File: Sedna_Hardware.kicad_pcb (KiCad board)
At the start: 2 copper layers, 82.8 x 90.4 mm, 51 parts, among them J1 PJ-102A, J10 5-103735-2, J11 5-103634-1, J2 61201021721, J3 PPTC141LFBN-RC, J4 0878340619, J5 5-103634-2, J6 5-103361-1, J7 1935161, J8 1935161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

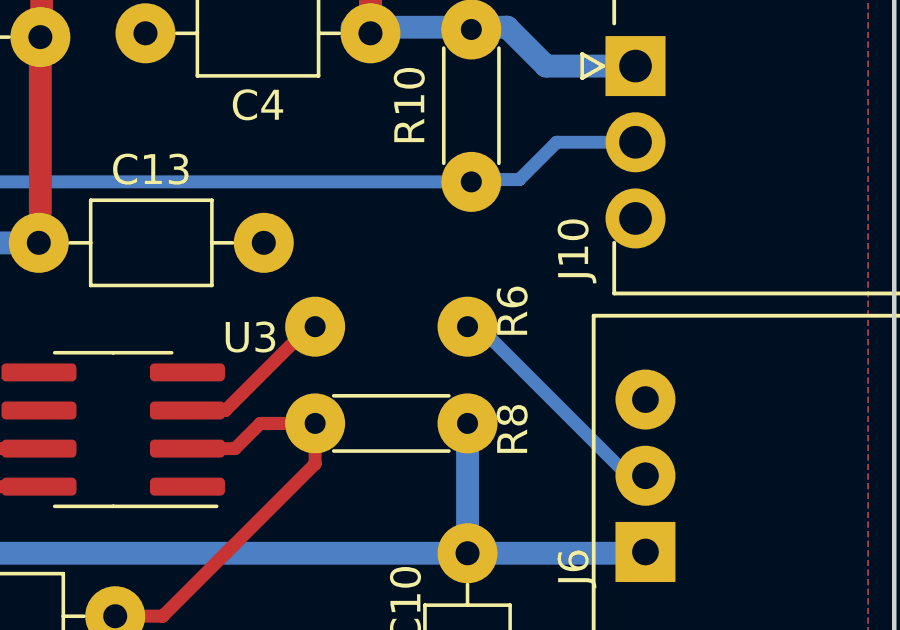
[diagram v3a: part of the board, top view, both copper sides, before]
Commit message: flipped resistor and power terminal to front plane
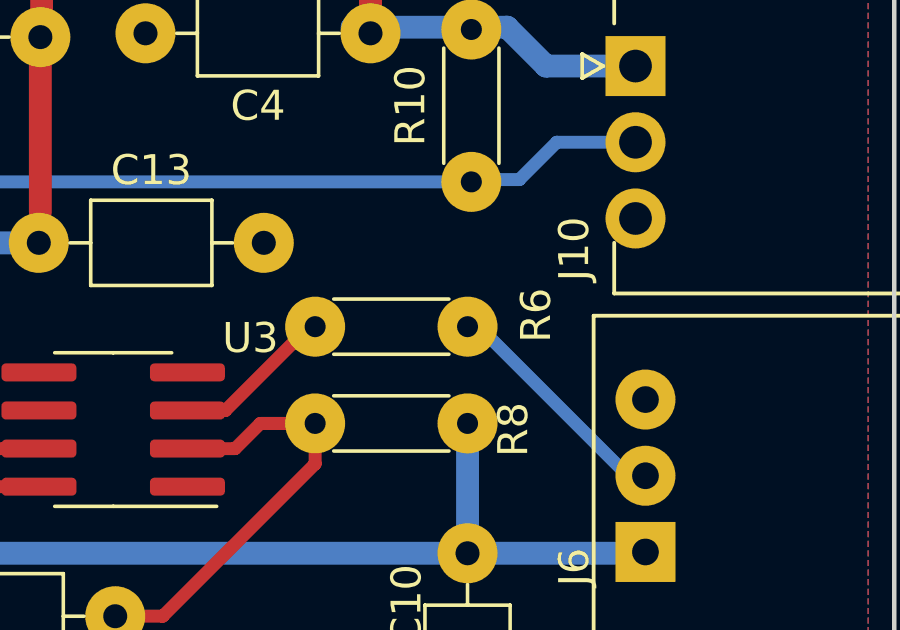
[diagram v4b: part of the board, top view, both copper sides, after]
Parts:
- R6: moved to F.Cu
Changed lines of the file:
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@@
+    )
+  )
+  (footprint "Resistor_THT:R_Axial_DIN0204_L3.6mm_D1.6mm_P5.08mm_Horizontal" (layer "F.Cu")
+    (at 171.176 128.347 180)
+    (descr "Resistor, Axial_DIN0204 series, Axial, Horizontal, pin pitch=5.08mm, 0.167W, length*diameter=3.6*1.6mm^2, http://cdn-reichelt.de/documents/datenblatt/B400/1_4W%23YAG.pdf")
+    (tags "Resistor Axial_DIN0204 series Axial Horizontal pin pitch 5.08mm 0.167W length 3.6mm diameter 1.6mm")
+    (property "Category" "Through Hole Resistors")
+    (property "DK_Datasheet_Link" "https://www.vishay.com/docs/28766/mbxsma.pdf")
+    (property "DK_Detail_Page" "https://www.digikey.ca/en/products/detail/vishay-beyschlag-draloric-bc-components/MBA02040C1002FRP00/336349")
+    (property "Description" "RES 10K OHM 0.4W 1% AXIAL")
+    (property "Digi-Key_PN" "BC10.0KXTR-ND")
+    (property "MPN" "MBA02040C1002FRP00")
+    (property "Manufacturer" "Vishay Beyschlag/Draloric/BC Components")
+    (property "Sheetfile" "Sedna_Hardware.kicad_sch")
+    (property "Sheetname" "")
+    (property "Status" "active")
+    (attr through_hole)
+    (fp_text reference "R6" (at -2.286 0.381 -90) (layer "F.SilkS")
+      (effects (font (size 1 1) (thickness 0.15)))
+    )
+    (fp_text value "10k" (at 2.54 1.92) (layer "F.Fab")
+      (effects (font (size 1 1) (thickness 0.15)))
+    )
+    (fp_text user "${REFERENCE}" (at 2.54 0) (layer "F.Fab")
+      (effects (font (size 0.72 0.72) (thickness 0.108)))
+    )
+    (fp_line (start 0.62 0.92) (end 4.46 0.92) (layer "F.SilkS") (width 0.12))
+    (fp_line (start 0.62 -0.92) (end 4.46 -0.92) (layer "F.SilkS") (width 0.12))
+    (fp_line (start 6.03 -1.05) (end -0.95 -1.05) (layer "F.CrtYd") (width 0.05))
+    (fp_line (start -0.95 -1.05) (end -0.95 1.05) (layer "F.CrtYd") (width 0.05))
+    (fp_line (start -0.95 1.05) (end 6.03 1.05) (layer "F.CrtYd") (width 0.05))
+    (fp_line (start 6.03 1.05) (end 6.03 -1.05) (layer "F.CrtYd") (width 0.05))
+    (fp_line (start 0.74 0.8) (end 4.34 0.8) (layer "F.Fab") (width 0.1))
+    (fp_line (start 0.74 -0.8) (end 0.74 0.8) (layer "F.Fab") (width 0.1))
+    (fp_line (start 5.08 0) (end 4.34 0) (layer "F.Fab") (width 0.1))
+    (fp_line (start 0 0) (end 0.74 0) (layer "F.Fab") (width 0.1))
+    (fp_line (start 4.34 -0.8) (end 0.74 -0.8) (layer "F.Fab") (width 0.1))
+    (fp_line (start 4.34 0.8) (end 4.34 -0.8) (layer "F.Fab") (width 0.1))
+    (pad "1" thru_hole circle (at 0 0 180) (size 2 2) (drill 0.7) (layers *.Cu *.Mask)
+      (net 21 "Net-(J6-Pad2)") (pintype "passive"))
+    (pad "2" thru_hole oval (at 5.08 0 180) (size 2 2) (drill 0.7) (layers *.Cu *.Mask)
+      (net 56 "Net-(R6-Pad2)") (pintype "passive"))
+    (model "${KICAD6_3DMODEL_DIR}/Resistor_THT.3dshapes/R_Axial_DIN0204_L3.6mm_D1.6mm_P5.08mm_Horizontal.wrl"
+      (offset (xyz 0 0 0))
+      (scale (xyz 1 1 1))
+      (rotate (xyz 0 0 0))
     )
   )
@@
       (net 35 "Net-(J7-Pad2)") (pintype "passive"))
   )
-  (footprint "Resistor_THT:R_Axial_DIN0204_L3.6mm_D1.6mm_P5.08mm_Horizontal" (layer "B.Cu")
-    (at 171.176 128.347 180)
-    (descr "Resistor, Axial_DIN0204 series, Axial, Horizontal, pin pitch=5.08mm, 0.167W, length*diameter=3.6*1.6mm^2, http://cdn-reichelt.de/documents/datenblatt/B400/1_4W%23YAG.pdf")
-    (tags "Resistor Axial_DIN0204 series Axial Horizontal pin pitch 5.08mm 0.167W length 3.6mm diameter 1.6mm")
-    (property "Category" "Through Hole Resistors")
-    (property "DK_Datasheet_Link" "https://www.vishay.com/docs/28766/mbxsma.pdf")
-    (property "DK_Detail_Page" "https://www.digikey.ca/en/products/detail/vishay-beyschlag-draloric-bc-components/MBA02040C1002FRP00/336349")
-    (property "Description" "RES 10K OHM 0.4W 1% AXIAL")
-    (property "Digi-Key_PN" "BC10.0KXTR-ND")
-    (property "MPN" "MBA02040C1002FRP00")
-    (property "Manufacturer" "Vishay Beyschlag/Draloric/BC Components")
-    (property "Sheetfile" "Sedna_Hardware.kicad_sch")
-    (property "Sheetname" "")
-    (property "Status" "active")
-    (attr through_hole)
-    (fp_text reference "R6" (at -1.524 0.508 90) (layer "F.SilkS")
-      (effects (font (size 1 1) (thickness 0.15)))
-    )
-    (fp_text value "10k" (at 2.54 -1.92) (layer "B.Fab")
-      (effects (font (size 1 1) (thickness 0.15)) (justify mirror))
-    )
-    (fp_text user "${REFERENCE}" (at 2.54 0) (layer "B.Fab")
-      (effects (font (size 0.72 0.72) (thickness 0.108)) (justify mirror))
-    )
-    (fp_line (start 0.62 -0.92) (end 4.46 -0.92) (layer "B.SilkS") (width 0.12))
-    (fp_line (start 0.62 0.92) (end 4.46 0.92) (layer "B.SilkS") (width 0.12))
-    (fp_line (start 6.03 1.05) (end -0.95 1.05) (layer "B.CrtYd") (width 0.05))
-    (fp_line (start -0.95 1.05) (end -0.95 -1.05) (layer "B.CrtYd") (width 0.05))
-    (fp_line (start -0.95 -1.05) (end 6.03 -1.05) (layer "B.CrtYd") (width 0.05))
-    (fp_line (start 6.03 -1.05) (end 6.03 1.05) (layer "B.CrtYd") (width 0.05))
-    (fp_line (start 0.74 -0.8) (end 4.34 -0.8) (layer "B.Fab") (width 0.1))
-    (fp_line (start 0.74 0.8) (end 0.74 -0.8) (layer "B.Fab") (width 0.1))
-    (fp_line (start 5.08 0) (end 4.34 0) (layer "B.Fab") (width 0.1))
-    (fp_line (start 0 0) (end 0.74 0) (layer "B.Fab") (width 0.1))
-    (fp_line (start 4.34 0.8) (end 0.74 0.8) (layer "B.Fab") (width 0.1))
-    (fp_line (start 4.34 -0.8) (end 4.34 0.8) (layer "B.Fab") (width 0.1))
-    (pad "1" thru_hole circle (at 0 0 180) (size 2 2) (drill 0.7) (layers *.Cu *.Mask)
-      (net 21 "Net-(J6-Pad2)") (pintype "passive"))
-    (pad "2" thru_hole oval (at 5.08 0 180) (size 2 2) (drill 0.7) (layers *.Cu *.Mask)
-      (net 56 "Net-(R6-Pad2)") (pintype "passive"))
-    (model "${KICAD6_3DMODEL_DIR}/Resistor_THT.3dshapes/R_Axial_DIN0204_L3.6mm_D1.6mm_P5.08mm_Horizontal.wrl"
-      (offset (xyz 0 0 0))
-      (scale (xyz 1 1 1))
-      (rotate (xyz 0 0 0))
-    )
-  )
   (gr_line (start 185.4 56.388) (end 102.616 56.388) (layer "Edge.Cuts") (width 0.15))
   (gr_line (start 102.616 56.388) (end 102.616 146.812) (layer "Edge.Cuts") (width 0.15))
@@
   (gr_line (start 115.829 142.511755) (end 115.824 67.056) (layer "User.2") (width 0.15))
   (gr_line (start 115.824 67.056) (end 101.092 67.056) (layer "User.2") (width 0.15))
-  (gr_line (start 120.904 54.356) (end 175.26 54.356) (layer "User.3") (width 0.15))
-  (gr_line (start 120.904 147.828) (end 120.904 54.356) (layer "User.3") (width 0.15))
-  (gr_line (start 175.26 54.356) (end 175.26 147.828) (layer "User.3") (width 0.15))
-  (gr_line (start 175.26 147.828) (end 120.904 147.828) (layer "User.3") (width 0.15))
   (segment (start 134.697 87.075) (end 134.657 87.115) (width 0.25) (layer "F.Cu") (net 1))
   (segment (start 152.507 88.977) (end 155.428 86.056) (width 1.0668) (layer "B.Cu") (net 1))
@@
     (polygon
       (pts
-        (xy 138.181 57.167762)
-        (xy 138.181 74.947762)
-        (xy 122.433 74.947762)
-        (xy 122.433 57.167762)
+        (xy 136.657 56.846)
+        (xy 136.657 74.626)
+        (xy 120.909 74.626)
+        (xy 120.909 56.846)
       )
     )

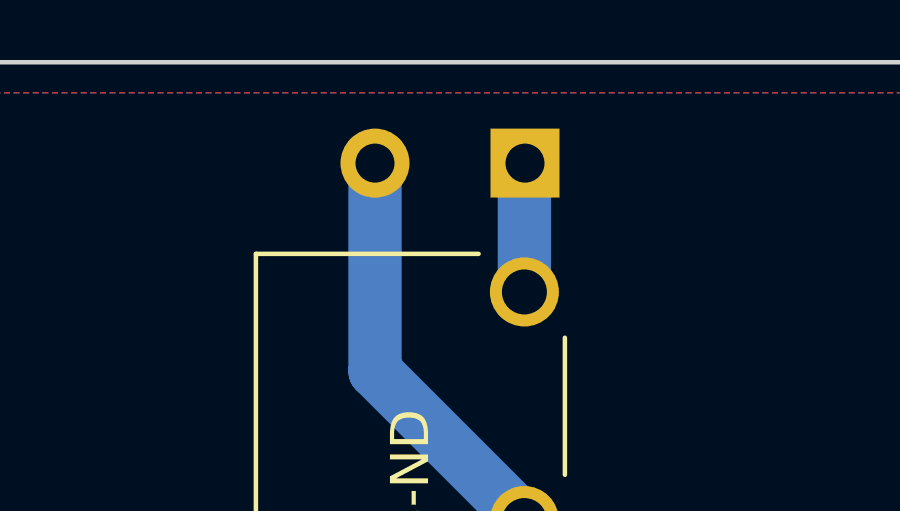
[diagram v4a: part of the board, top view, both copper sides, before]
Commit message: oopus forgot to flip power terminal to front plane
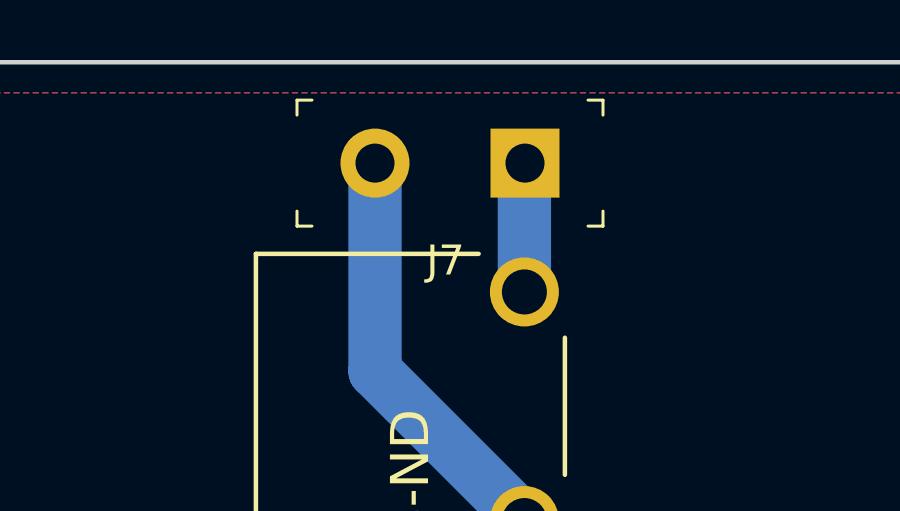
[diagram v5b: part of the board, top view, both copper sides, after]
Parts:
- J7: moved to F.Cu
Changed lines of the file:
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@@
     )
+  )
+  (footprint "digikey-footprints:Terminal_Block_D1.3mm_P5mm" (layer "F.Cu")
+    (at 156.2 59.75 180)
+    (descr "https://media.digikey.com/pdf/Data%20Sheets/Phoenix%20Contact%20PDFs/1935161.pdf")
+    (property "Category" "Connectors, Interconnects")
+    (property "DK_Datasheet_Link" "https://media.digikey.com/pdf/Data%20Sheets/Phoenix%20Contact%20PDFs/1935161.pdf")
+    (property "DK_Detail_Page" "/product-detail/en/phoenix-contact/1935161/277-1667-ND/568614")
+    (property "Description" "TERM BLK 2POS SIDE ENTRY 5MM PCB")
+    (property "Digi-Key_PN" "277-1667-ND")
+    (property "Family" "Terminal Blocks - Wire to Board")
+    (property "MPN" "1935161")
+    (property "Manufacturer" "Phoenix Contact")
+    (property "Sheetfile" "Sedna_Hardware.kicad_sch")
+    (property "Sheetname" "")
+    (property "Status" "Active")
+    (attr through_hole)
+    (fp_text reference "J7" (at 2.65 -3.25) (layer "F.SilkS")
+      (effects (font (size 1 1) (thickness 0.15)))
+    )
+    (fp_text value "1935161" (at 2.35 3.6) (layer "F.Fab")
+      (effects (font (size 1 1) (thickness 0.15)))
+    )
+    (fp_text user "${REFERENCE}" (at 2.3 0) (layer "F.Fab")
+      (effects (font (size 1 1) (thickness 0.15)))
+    )
+    (fp_line (start 7.6 2.1) (end 7.6 1.6) (layer "F.SilkS") (width 0.1))
+    (fp_line (start -2.6 2.1) (end -2.6 1.6) (layer "F.SilkS") (width 0.1))
+    (fp_line (start 7.6 -2.1) (end 7.1 -2.1) (layer "F.SilkS") (width 0.1))
+    (fp_line (start 7.6 2.1) (end 7.1 2.1) (layer "F.SilkS") (width 0.1))
+    (fp_line (start -2.6 -2.1) (end -2.6 -1.6) (layer "F.SilkS") (width 0.1))
+    (fp_line (start 7.6 -2.1) (end 7.6 -1.6) (layer "F.SilkS") (width 0.1))
+    (fp_line (start -2.6 -2.1) (end -2.1 -2.1) (layer "F.SilkS") (width 0.1))
+    (fp_line (start -2.6 2.1) (end -2.1 2.1) (layer "F.SilkS") (width 0.1))
+    (fp_line (start 7.75 -2.25) (end 7.75 2.25) (layer "F.CrtYd") (width 0.05))
+    (fp_line (start -2.75 2.25) (end 7.75 2.25) (layer "F.CrtYd") (width 0.05))
+    (fp_line (start -2.75 -2.25) (end 7.75 -2.25) (layer "F.CrtYd") (width 0.05))
+    (fp_line (start -2.75 -2.25) (end -2.75 2.25) (layer "F.CrtYd") (width 0.05))
+    (fp_line (start -2.5 2) (end 7.5 2) (layer "F.Fab") (width 0.1))
+    (fp_line (start 7.5 -2) (end 7.5 2) (layer "F.Fab") (width 0.1))
+    (fp_line (start -2.5 -2) (end -2.5 2) (layer "F.Fab") (width 0.1))
+    (fp_line (start -2.5 -2) (end 7.5 -2) (layer "F.Fab") (width 0.1))
+    (pad "1" thru_hole rect locked (at 0 0 180) (size 2.3 2.3) (drill 1.3) (layers *.Cu *.Mask)
+      (net 36 "Net-(J7-Pad1)") (pintype "passive"))
+    (pad "2" thru_hole circle locked (at 5 0 180) (size 2.3 2.3) (drill 1.3) (layers *.Cu *.Mask)
+      (net 35 "Net-(J7-Pad2)") (pintype "passive"))
   )
   (footprint "Diode_THT:D_DO-41_SOD81_P10.16mm_Horizontal" (layer "F.Cu")
@@
     )
   )
-  (footprint "digikey-footprints:Terminal_Block_D1.3mm_P5mm" (layer "B.Cu")
-    (at 156.2 59.75 180)
-    (descr "https://media.digikey.com/pdf/Data%20Sheets/Phoenix%20Contact%20PDFs/1935161.pdf")
-    (property "Category" "Connectors, Interconnects")
-    (property "DK_Datasheet_Link" "https://media.digikey.com/pdf/Data%20Sheets/Phoenix%20Contact%20PDFs/1935161.pdf")
-    (property "DK_Detail_Page" "/product-detail/en/phoenix-contact/1935161/277-1667-ND/568614")
-    (property "Description" "TERM BLK 2POS SIDE ENTRY 5MM PCB")
-    (property "Digi-Key_PN" "277-1667-ND")
-    (property "Family" "Terminal Blocks - Wire to Board")
-    (property "MPN" "1935161")
-    (property "Manufacturer" "Phoenix Contact")
-    (property "Sheetfile" "Sedna_Hardware.kicad_sch")
-    (property "Sheetname" "")
-    (property "Status" "Active")
-    (attr through_hole)
-    (fp_text reference "J7" (at 2.65 3.25) (layer "B.SilkS")
-      (effects (font (size 1 1) (thickness 0.15)) (justify mirror))
-    )
-    (fp_text value "1935161" (at 2.35 -3.6) (layer "B.Fab")
-      (effects (font (size 1 1) (thickness 0.15)) (justify mirror))
-    )
-    (fp_text user "${REFERENCE}" (at 2.3 0) (layer "B.Fab")
-      (effects (font (size 1 1) (thickness 0.15)) (justify mirror))
-    )
-    (fp_line (start 7.6 -2.1) (end 7.6 -1.6) (layer "B.SilkS") (width 0.1))
-    (fp_line (start -2.6 -2.1) (end -2.6 -1.6) (layer "B.SilkS") (width 0.1))
-    (fp_line (start 7.6 2.1) (end 7.1 2.1) (layer "B.SilkS") (width 0.1))
-    (fp_line (start 7.6 -2.1) (end 7.1 -2.1) (layer "B.SilkS") (width 0.1))
-    (fp_line (start -2.6 2.1) (end -2.6 1.6) (layer "B.SilkS") (width 0.1))
-    (fp_line (start 7.6 2.1) (end 7.6 1.6) (layer "B.SilkS") (width 0.1))
-    (fp_line (start -2.6 2.1) (end -2.1 2.1) (layer "B.SilkS") (width 0.1))
-    (fp_line (start -2.6 -2.1) (end -2.1 -2.1) (layer "B.SilkS") (width 0.1))
-    (fp_line (start 7.75 2.25) (end 7.75 -2.25) (layer "B.CrtYd") (width 0.05))
-    (fp_line (start -2.75 -2.25) (end 7.75 -2.25) (layer "B.CrtYd") (width 0.05))
-    (fp_line (start -2.75 2.25) (end 7.75 2.25) (layer "B.CrtYd") (width 0.05))
-    (fp_line (start -2.75 2.25) (end -2.75 -2.25) (layer "B.CrtYd") (width 0.05))
-    (fp_line (start -2.5 -2) (end 7.5 -2) (layer "B.Fab") (width 0.1))
-    (fp_line (start 7.5 2) (end 7.5 -2) (layer "B.Fab") (width 0.1))
-    (fp_line (start -2.5 2) (end -2.5 -2) (layer "B.Fab") (width 0.1))
-    (fp_line (start -2.5 2) (end 7.5 2) (layer "B.Fab") (width 0.1))
-    (pad "1" thru_hole rect locked (at 0 0 180) (size 2.3 2.3) (drill 1.3) (layers *.Cu *.Mask)
-      (net 36 "Net-(J7-Pad1)") (pintype "passive"))
-    (pad "2" thru_hole circle locked (at 5 0 180) (size 2.3 2.3) (drill 1.3) (layers *.Cu *.Mask)
-      (net 35 "Net-(J7-Pad2)") (pintype "passive"))
-  )
   (gr_line (start 185.4 56.388) (end 102.616 56.388) (layer "Edge.Cuts") (width 0.15))
